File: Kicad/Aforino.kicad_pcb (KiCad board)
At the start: 2 copper layers, 5 parts, among them SW1 SW_Push, U1 ESP-Breatout-16Pin

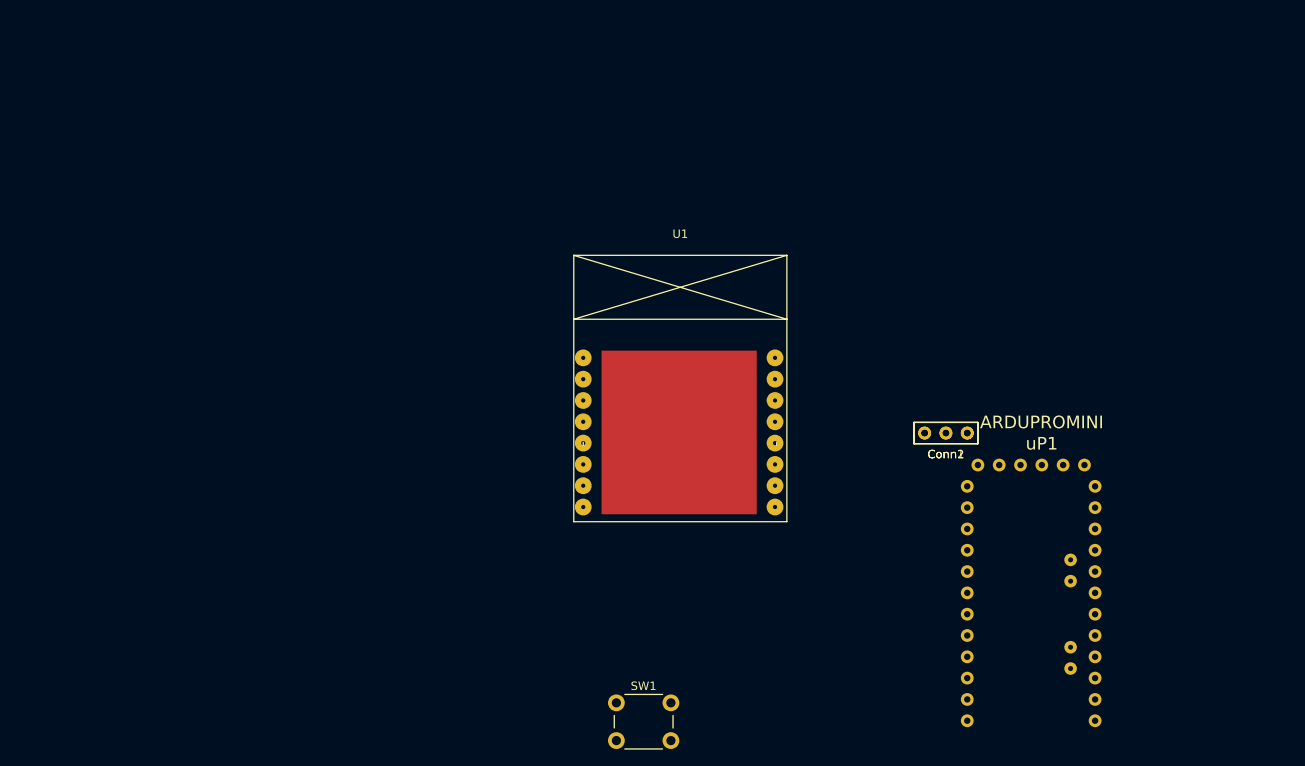
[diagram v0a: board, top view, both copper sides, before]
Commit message: Under Contruction: Kicad Pcbnew, Track and Vias
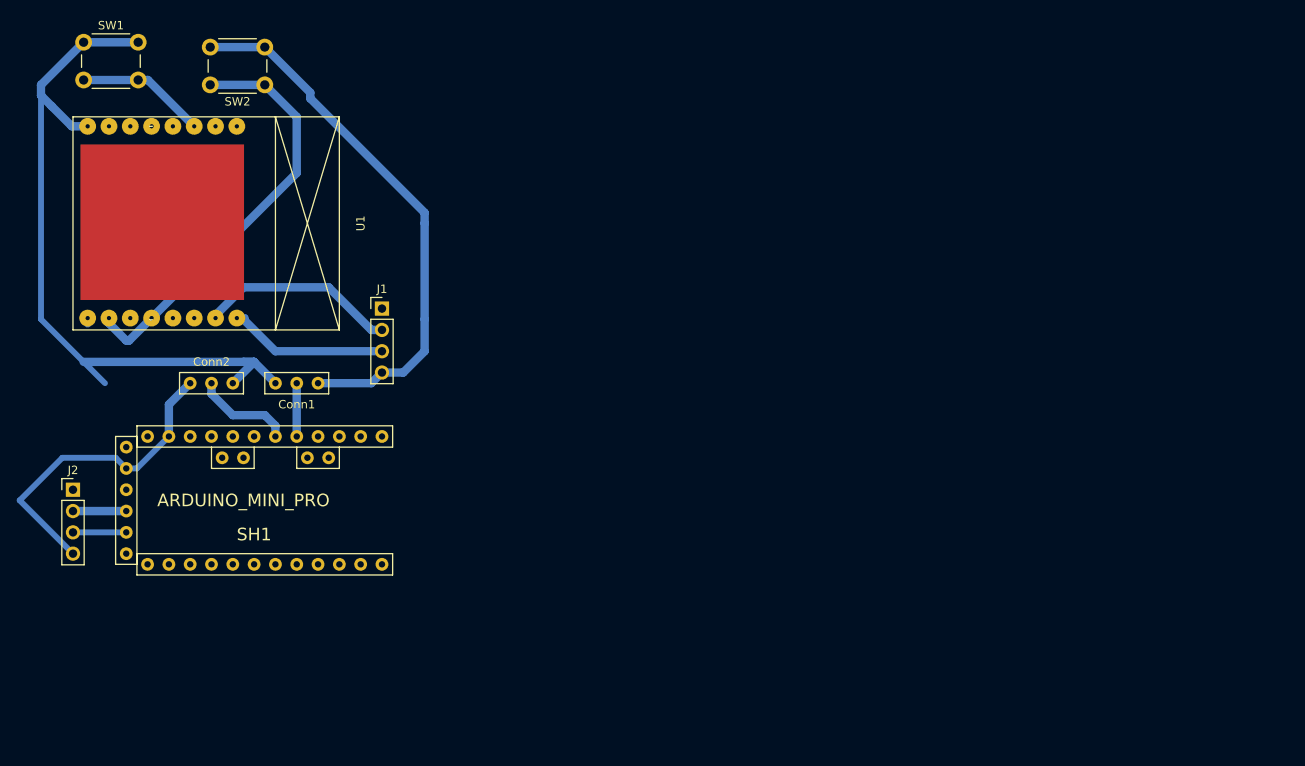
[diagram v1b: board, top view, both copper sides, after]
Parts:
- removed uP1: ARDUPROMINI, ArduProMiniTKB:ArduProMini
- added J1: Conn_01x04_Female, Connector_PinHeader_2.54mm:PinHeader_1x04_P2.54mm_Vertical, F.Cu at (81.3, 90.2)
- added J2: Conn_01x04_Female, Connector_PinHeader_2.54mm:PinHeader_1x04_P2.54mm_Vertical, F.Cu at (44.5, 111.8)
- added SH1: ARDUINO_MINI_PRO, SHIELD_ARDUINO:ARDUINO_MINI_PRO_V10, F.Cu at (66.0, 113.0)
- added SW2: SW_Push, Buttons_Switches_THT:SW_PUSH_6mm_h5mm, F.Cu at (67.3, 63.5)
- SW1: footprint Button_Switch_THT:SW_PUSH_6mm_h5mm -> Buttons_Switches_THT:SW_PUSH_6mm_h5mm
- moved SW1 101.2 mm to (45.7, 58.4)
- moved Conn2 87.7 mm to (61.0, 99.1), turned to 180 degrees
- moved Conn1 77.6 mm to (71.1, 99.1)
- moved U1 65.6 mm to (55.9, 80.0), turned to 270 degrees
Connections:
- SW1 pad 1: Net-(SW1-Pad1) -> +3V3
- SW1 pad 2: Net-(SW1-Pad2) -> /FIRM_SW
- U1 pad 10: (no net) -> Net-(SW2-Pad1)
- U1 pad 11: (no net) -> /FIRM_SW
- U1 pad 12: (no net) -> Net-(SW2-Pad1)
- U1 pad 13: (no net) -> /SCL
- U1 pad 14: (no net) -> /SDA
- U1 pad 15: (no net) -> Net-(J1-Pad2)
- U1 pad 16: (no net) -> Net-(J1-Pad3)
- U1 pad 3: (no net) -> /FIRM_SW
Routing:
- net GND: track 0.00 -> 104.2 mm
- net +3V3: track 0.00 -> 90.1 mm
- net Net-(SW2-Pad1): track 0.00 -> 50.7 mm
- net Net-(J1-Pad2): track 0.00 -> 23.7 mm
- net Net-(J1-Pad3): track 0.00 -> 19.9 mm
- net /FIRM_SW: track 0.00 -> 15.5 mm
- net /IR_OUT: track 0.00 -> 11.7 mm
- net Net-(J2-Pad3): track 0.00 -> 6.35 mm
- net Net-(J2-Pad2): track 0.00 -> 6.35 mm
- net /IR_IN: track 0.00 -> 6.35 mm

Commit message: Kidcat first testing board
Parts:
- added LM2596-1: myConn_LM2596_Male, myLib:myConn_LM2596_Male, F.Cu at (170.2, 82.5)
- SW1, SW2: footprint Buttons_Switches_THT:SW_PUSH_6mm_h5mm -> Buttons_Switches_THT:SW_PUSH_6mm
- moved J2 136.7 mm to (180.3, 96.5), turned to 180 degrees
- moved SH1 94.2 mm to (158.8, 96.5), turned to 270 degrees
- moved Conn1 90.0 mm to (160.0, 113.0), turned to 270 degrees
- moved Conn2 90.0 mm to (149.9, 113.0), turned to 270 degrees
- moved SW2 62.3 mm to (127.0, 81.3)
- moved SW1 61.1 mm to (104.1, 76.2)
- moved U1 61.0 mm to (113.7, 99.7)
- moved J1 56.4 mm to (135.9, 104.1)
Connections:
- SH1 pad GND2: (no net) -> GND
- SH1 pad GND3: GND -> (no net)
- SH1 pad VCC1: (no net) -> +3V3
- SH1 pad VCC2: +3V3 -> (no net)
- U1 pad 13: /SCL -> /SDA
- U1 pad 14: /SDA -> /SCL
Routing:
- net GND: track 104.2 -> 242.8 mm
- net +3V3: track 90.1 -> 185.1 mm
- net /SDA: track 0.00 -> 63.4 mm
- net /SCL: track 0.00 -> 57.9 mm
- net /IR_IN: track 6.35 -> 55.8 mm
- net /FIRM_SW: track 15.5 -> 55.5 mm
- net /IR_OUT: track 11.7 -> 43.1 mm
- net Net-(SW2-Pad1): track 50.7 -> 59.3 mm
- net Net-(J1-Pad2): track 23.7 -> 19.7 mm
- net Net-(J1-Pad3): track 19.9 -> 16.3 mm
- net Net-(J2-Pad3): track 6.35 -> 6.88 mm
- net Net-(J2-Pad2): track 6.35 -> 6.88 mm
- added copper zone on B.Cu, net GND
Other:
- board outline added: 88.9 x 50.8 mm
- net class Default: trace_width 1 -> 0.7

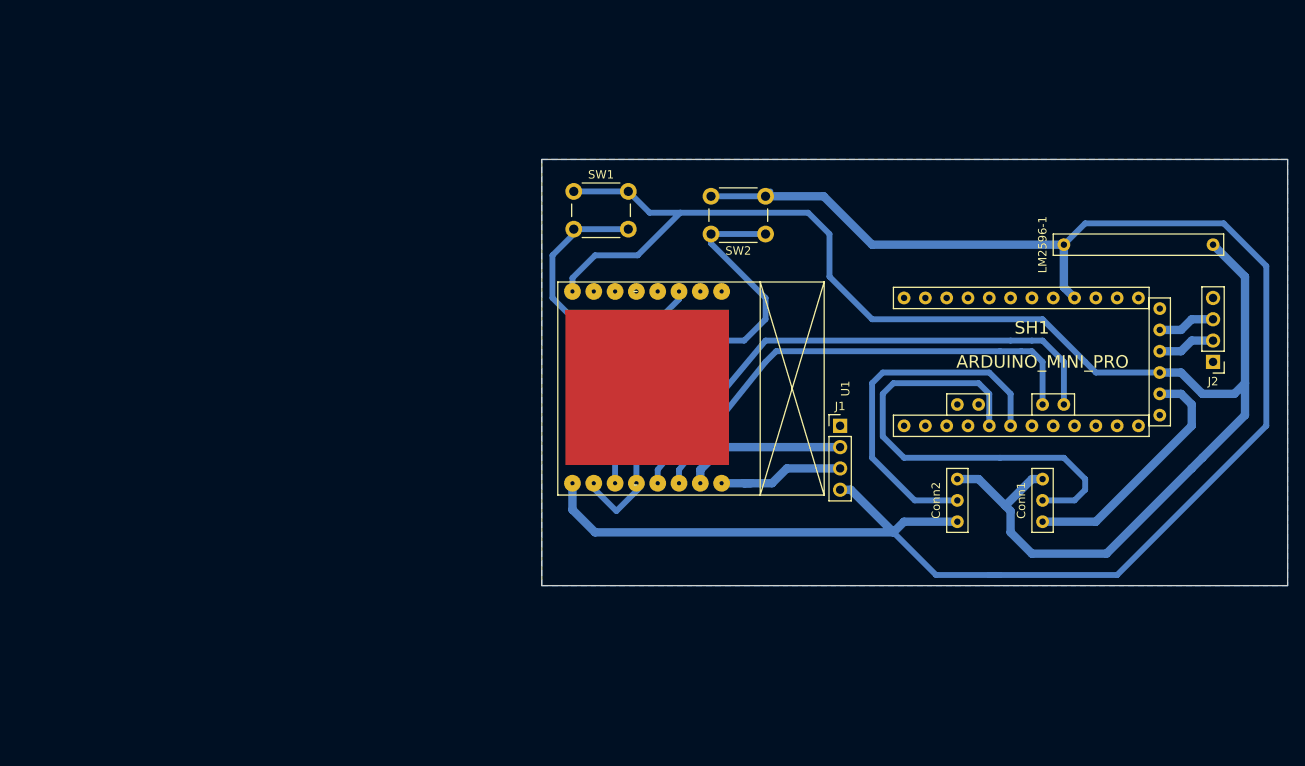
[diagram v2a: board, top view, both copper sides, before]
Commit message: Kicad: ESP8266 Breakout Shield Good! Jumpers to Upload firmware! Best component order!
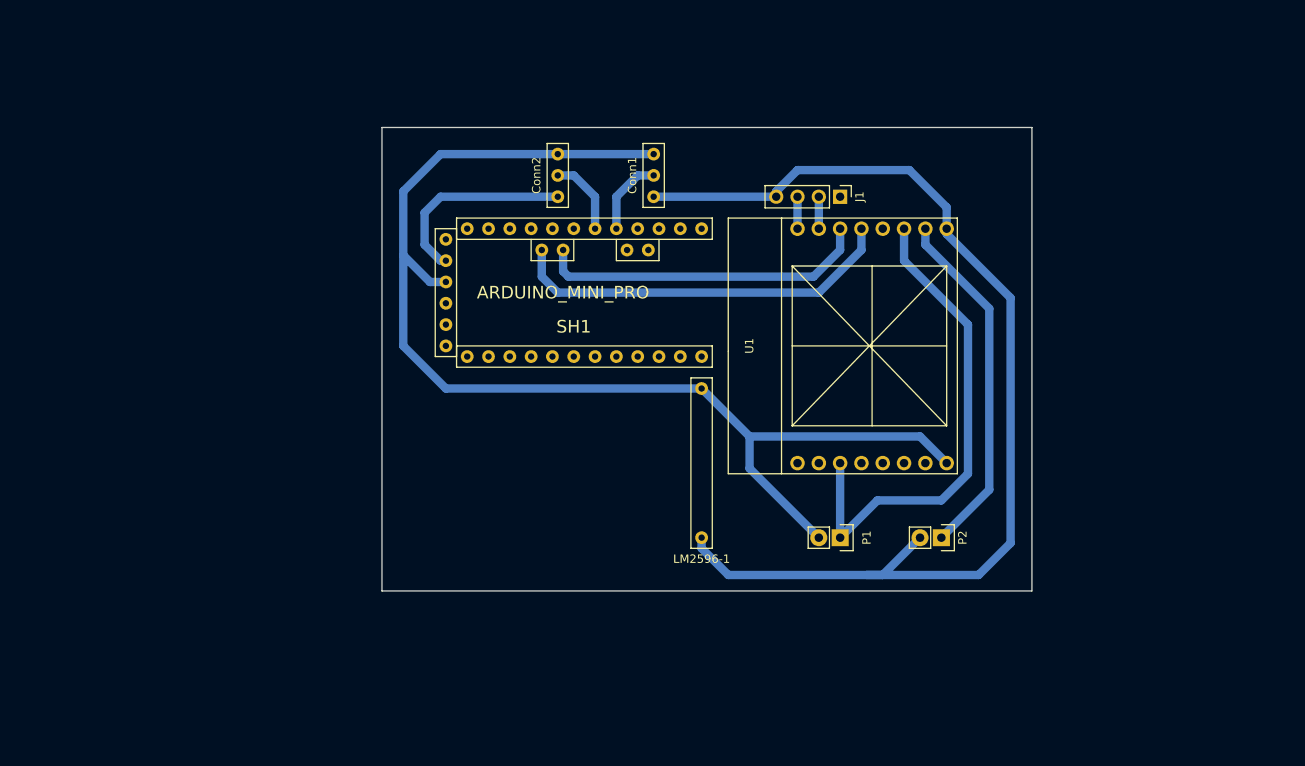
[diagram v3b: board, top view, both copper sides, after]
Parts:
- removed J2: Conn_01x04_Female, Connector_PinHeader_2.54mm:PinHeader_1x04_P2.54mm_Vertical
- removed SW1, SW2: SW_Push, Buttons_Switches_THT:SW_PUSH_6mm
- added P1: CONN_01X02, Pin_Headers:Pin_Header_Straight_1x02, F.Cu at (135.9, 117.5)
- added P2: CONN_01X02, Pin_Headers:Pin_Header_Straight_1x02, F.Cu at (148.0, 117.5)
- U1: footprint myLib:ESP-Breakout-16PIN -> Escolabs:ESP8266-Breakout_Board-16Pin
- moved Conn2 61.4 mm to (102.2, 74.3)
- moved Conn1 60.4 mm to (113.7, 74.3)
- moved LM2596-1 57.7 mm to (119.4, 109.9), turned to 0 degrees
- moved SH1 55.2 mm to (104.1, 88.3), turned to 90 degrees
- moved J1 27.3 mm to (135.9, 76.8), turned to 270 degrees
- moved U1 19.3 mm to (130.8, 108.6), turned to 90 degrees
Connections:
- SH1 pad GND2: GND -> (no net)
- SH1 pad RX/1: Net-(J2-Pad2) -> (no net)
- SH1 pad TX/1: Net-(J2-Pad3) -> (no net)
- U1 pad 10: Net-(SW2-Pad1) -> /FIRM_SW
- U1 pad 11: /FIRM_SW -> Net-(P2-Pad1)
- U1 pad 12: Net-(SW2-Pad1) -> /SDA
- U1 pad 13: /SDA -> /SCL
- U1 pad 14: /SCL -> Net-(J1-Pad2)
- U1 pad 15: Net-(J1-Pad2) -> Net-(J1-Pad3)
- U1 pad 2: (no net) -> /FIRM_SW
- U1 pad 3: /FIRM_SW -> (no net)
- U1 pad 7: (no net) -> +3V3
- U1 pad 8: +3V3 -> GND
- U1 pad 9: GND -> Net-(P2-Pad1)
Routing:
- net GND: track 242.8 -> 154.6 mm
- net Net-(SW2-Pad1): track 59.3 -> 0.00 mm
- net /IR_IN: track 55.8 -> 9.31 mm
- net +3V3: track 185.1 -> 142.5 mm
- net Net-(P2-Pad1): track 0.00 -> 42.4 mm
- net /IR_OUT: track 43.1 -> 9.31 mm
- net /SCL: track 57.9 -> 39.7 mm
- net /SDA: track 63.4 -> 46.7 mm
- net Net-(J1-Pad2): track 19.7 -> 3.81 mm
- net Net-(J1-Pad3): track 16.3 -> 3.81 mm
- net Net-(J2-Pad3): track 6.88 -> 0.00 mm
- net Net-(J2-Pad2): track 6.88 -> 0.00 mm
- net /FIRM_SW: track 55.5 -> 60.3 mm
- removed copper zone on B.Cu, net GND
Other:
- board size 88.9 x 50.8 mm -> 77.5 x 55.2 mm
- net class Default: trace_width 0.7 -> 1
- net class Slim Track added: clearance 0.2, trace_width 0.7, via_dia 2, via_drill 0.4
